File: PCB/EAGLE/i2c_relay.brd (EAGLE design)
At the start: 49.5 x 87.3 mm, 67 parts, among them IC1 PCF8575TS_1,118, K1 G3MB-202PL-DC5, K2 G3MB-202PL-DC5, K3 G3MB-202PL-DC5, K4 G3MB-202PL-DC5, K5 G3MB-202PL-DC5, K6 G3MB-202PL-DC5, K7 G3MB-202PL-DC5, K8 G3MB-202PL-DC5, Q1 MMST2222A-7-F, Q2 MMST2222A-7-F, Q3 MMST2222A-7-F, Q4 MMST2222A-7-F, Q5 MMST2222A-7-F, Q6 MMST2222A-7-F, Q7 MMST2222A-7-F, Q8 MMST2222A-7-F

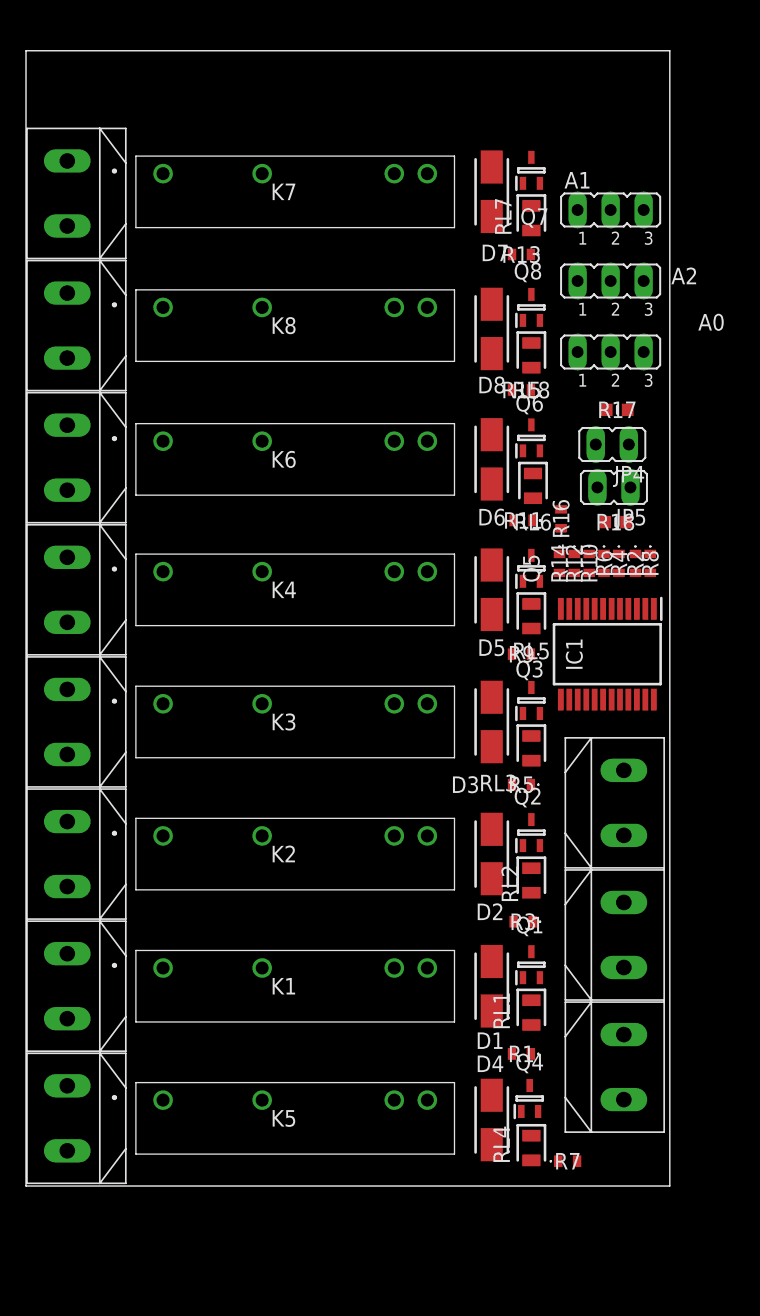
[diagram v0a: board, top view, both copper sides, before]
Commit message: FEAT: add 3d and push to FUSION360
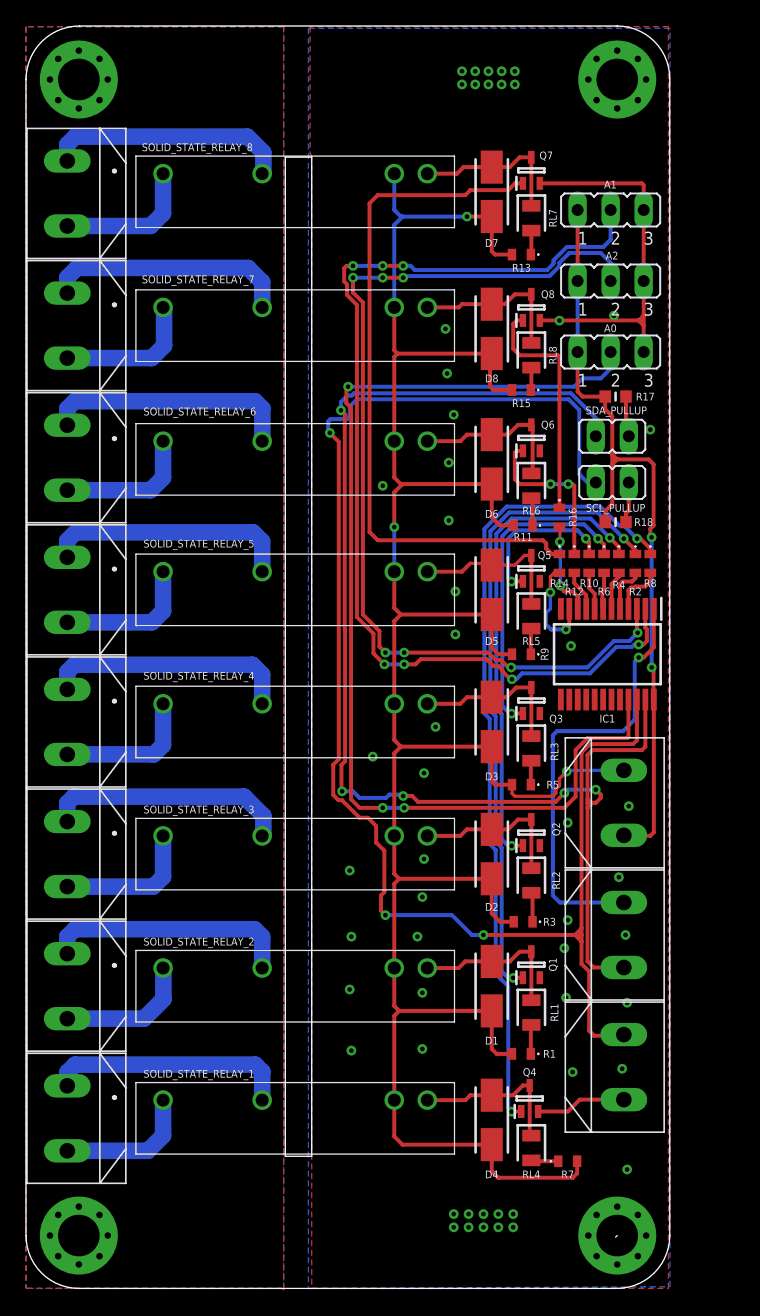
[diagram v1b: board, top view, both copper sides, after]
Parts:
- removed JP4, JP5: (no value), jumper:JP1
- added H1, H2, H3, H4: 3MM_HOLE, 3mm_special_hole:3MM_HOLE
- added SCL_PULLUP, SDA_PULLUP: (no value), jumper:JP1
- moved R17 1.02 mm to (45.3, 60.7)
- moved R11 0.38 mm to (38.2, 50.8)
- moved R16 0.18 mm to (41.0, 51.4), turned to 270 degrees
- moved RL6 0.13 mm to (38.9, 53.8)
- renumbered K1 to SOLID_STATE_RELAY_2, K2 to SOLID_STATE_RELAY_3, K3 to SOLID_STATE_RELAY_4, K4 to SOLID_STATE_RELAY_5, K5 to SOLID_STATE_RELAY_1, K6 to SOLID_STATE_RELAY_6, K7 to SOLID_STATE_RELAY_8, K8 to SOLID_STATE_RELAY_7
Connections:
- net +5V: now also U$11.1; no longer U$11.2
- net GND: now also U$9.2; no longer U$9.1
- net INT: now also U$10.1; no longer U$10.2
- net N$25: now also SDA_PULLUP.1; no longer JP4.1
- net N$27: now also SCL_PULLUP.1; no longer JP5.1
- net RELAY6: now also R16.2; no longer R14.2
- net RELAY7: now also R14.2; no longer R16.2
- net SCL: now also SCL_PULLUP.2, U$9.1; no longer JP5.2, U$9.2
- net SDA: now also SDA_PULLUP.2, U$10.2; no longer JP4.2, U$10.1
- net VCC: now also U$11.2; no longer U$11.1
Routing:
- net +5V: track 0.00 -> 185.5 mm, vias 0 -> 3
- net SCL: track 0.00 -> 117.6 mm, vias 0 -> 3
- net SDA: track 0.00 -> 102.8 mm, vias 0 -> 5
- net A0: track 0.00 -> 82.8 mm, vias 0 -> 3
- net A1: track 0.00 -> 80.6 mm, vias 0 -> 7
- net A2: track 0.00 -> 75.2 mm, vias 0 -> 7
- net N$12: track 0.00 -> 61.7 mm, vias 0 -> 2
- net VCC: track 0.00 -> 61.3 mm, vias 0 -> 2
- net N$21: track 0.00 -> 53.2 mm
- net N$3: track 0.00 -> 49.3 mm, vias 0 -> 2
- net N$6: track 0.00 -> 36.9 mm, vias 0 -> 2
- net GND: track 0.00 -> 36.5 mm, vias 0 -> 55
- net INT: track 0.00 -> 34.1 mm, vias 0 -> 1
- net N$9: track 0.00 -> 24.5 mm, vias 0 -> 2
- net NO5: track 0.00 -> 19.3 mm
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- added copper zone on layer 1, net 1
- added copper zone on layer 16, net 2
- added copper zone on layer 1, net GND
- added copper zone on layer 16, net GND
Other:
- board size 49.5 x 87.3 mm -> 49.5 x 97.1 mm
